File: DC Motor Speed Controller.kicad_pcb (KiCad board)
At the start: 2 copper layers, 64.8 x 30.8 mm, 15 parts, among them J1 Screw_Terminal_01x02, J2 Screw_Terminal_01x02, Q1 TIP122, U1 NE555P

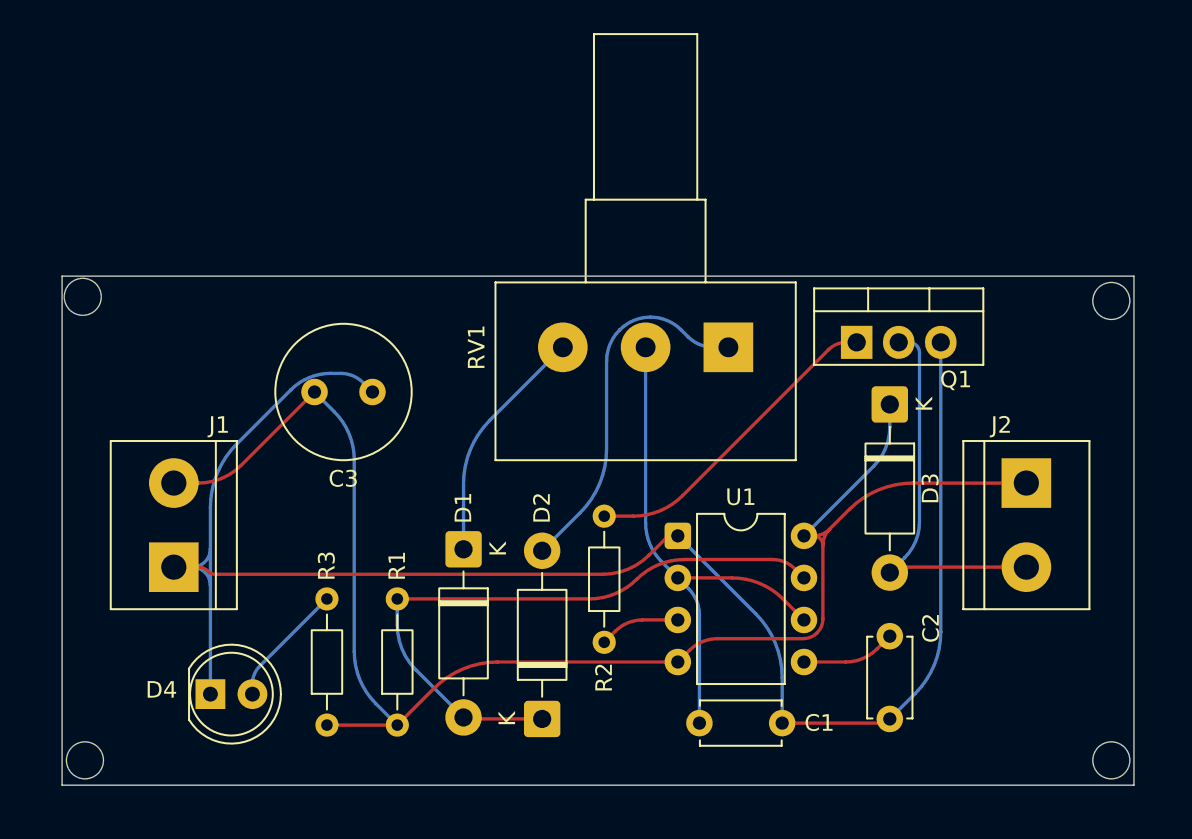
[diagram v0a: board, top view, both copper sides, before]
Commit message: Completed PCB -- Remaining Datasheets to Add
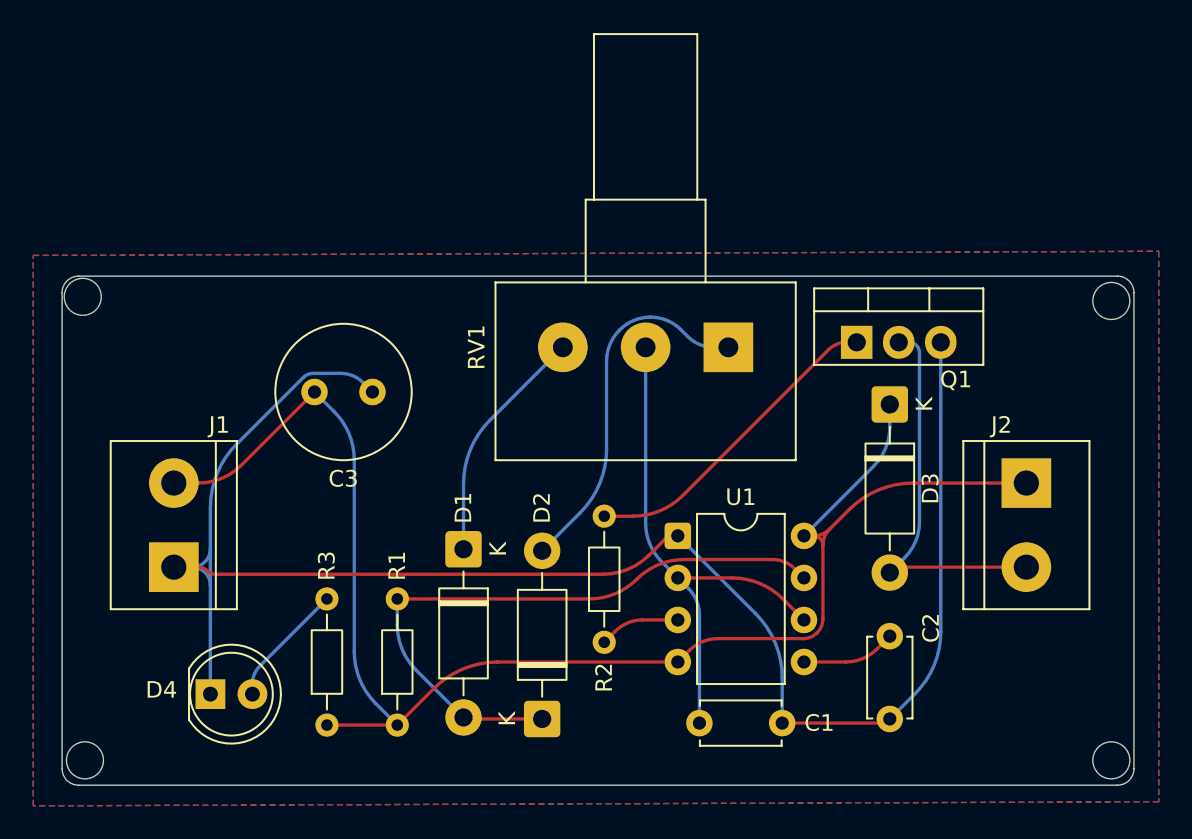
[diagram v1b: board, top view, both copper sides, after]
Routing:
- added copper zone on B.Cu, net GND
- added copper zone on F.Cu, net GND
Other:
- outline, holes or cut-outs redrawn
- board text added: "DC Motor Speed Controller"
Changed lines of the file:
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@@
 		)
+	)
+	(gr_line
+		(start 121.25 80.75)
+		(end 184 80.75)
+		(stroke
+			(width 0.05)
+			(type default)
+		)
+		(layer "Edge.Cuts")
+	)
+	(gr_arc
+		(start 185 110.5)
+		(mid 184.707107 111.207107)
+		(end 184 111.5)
+		(stroke
+			(width 0.05)
+			(type default)
+		)
+		(layer "Edge.Cuts")
 	)
 	(gr_circle
@@
 		(layer "Edge.Cuts")
 	)
-	(gr_rect
-		(start 120.25 80.75)
-		(end 185 111.5)
-		(stroke
-			(width 0.05)
-			(type default)
-		)
-		(fill no)
+	(gr_line
+		(start 120.25 110.5)
+		(end 120.25 81.75)
+		(stroke
+			(width 0.05)
+			(type default)
+		)
+		(layer "Edge.Cuts")
+	)
+	(gr_arc
+		(start 120.25 81.75)
+		(mid 120.542893 81.042893)
+		(end 121.25 80.75)
+		(stroke
+			(width 0.05)
+			(type default)
+		)
 		(layer "Edge.Cuts")
 	)
@@
 		(layer "Edge.Cuts")
 	)
+	(gr_arc
+		(start 184 80.75)
+		(mid 184.707107 81.042893)
+		(end 185 81.75)
+		(stroke
+			(width 0.05)
+			(type default)
+		)
+		(layer "Edge.Cuts")
+	)
 	(gr_circle
 		(center 183.631966 82.25)
@@
 		(layer "Edge.Cuts")
 	)
+	(gr_line
+		(start 184 111.5)
+		(end 121.25 111.5)
+		(stroke
+			(width 0.05)
+			(type default)
+		)
+		(layer "Edge.Cuts")
+	)
 	(gr_circle
 		(center 121.5 82)
@@
 		(layer "Edge.Cuts")
 	)
+	(gr_arc
+		(start 121.25 111.5)
+		(mid 120.542893 111.207107)
+		(end 120.25 110.5)
+		(stroke
+			(width 0.05)
+			(type default)
+		)
+		(layer "Edge.Cuts")
+	)
+	(gr_line
+		(start 185 81.75)
+		(end 185 110.5)
+		(stroke
+			(width 0.05)
+			(type default)
+		)
+		(layer "Edge.Cuts")
+	)
+	(gr_text "DC Motor Speed Controller"
+		(at 158.5 110.5 0)
+		(layer "B.SilkS")
+		(effects
+			(font
+				(size 1.5 1)
+				(thickness 0.2)
+				(bold yes)
+			)
+			(justify left bottom mirror)
+		)
+	)
 	(segment
 		(start 170.125 107.625)
@@
 	(segment
 		(start 130.803792 90.885207)
-		(end 134.072039 87.61696)
+		(end 134.810123 86.878876)
 		(width 0.2)
 		(layer "B.Cu")
@@
 	)
 	(segment
-		(start 136.4695 86.6239)
+		(start 135.42569 86.6239)
 		(end 137.077627 86.6239)
 		(width 0.2)
@@
 	)
 	(arc
-		(start 136.4695 86.6239)
-		(mid 135.172003 86.881987)
-		(end 134.072039 87.61696)
+		(start 135.42569 86.6239)
+		(mid 135.092548 86.690166)
+		(end 134.810123 86.878876)
 		(width 0.2)
 		(layer "B.Cu")
@@
 		(net 11)
 	)
+	(zone
+		(net 1)
+		(net_name "GND")
+		(layers "F.Cu" "B.Cu")
+		(hatch edge 0.5)
+		(connect_pads
+			(clearance 0.5)
+		)
+		(min_thickness 0.25)
+		(filled_areas_thickness no)
+		(fill yes
+			(thermal_gap 0.5)
+			(thermal_bridge_width 0.5)
+		)
+		(polygon
+			(pts
+				(xy 118.5 79.5) (xy 186.5 79.25) (xy 186.5 112.5) (xy 118.5 112.75)
+			)
+		)
+	)
 	(embedded_fonts no)
